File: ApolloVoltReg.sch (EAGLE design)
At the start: 24 parts, among them IC2 LM324D, J1 SSM-108-L-DV-BE-K-APOLLO, U1 TEXAS_INSTRUMENTS_PTH04070WAD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, U2 ACS712ELCTR-05B-T

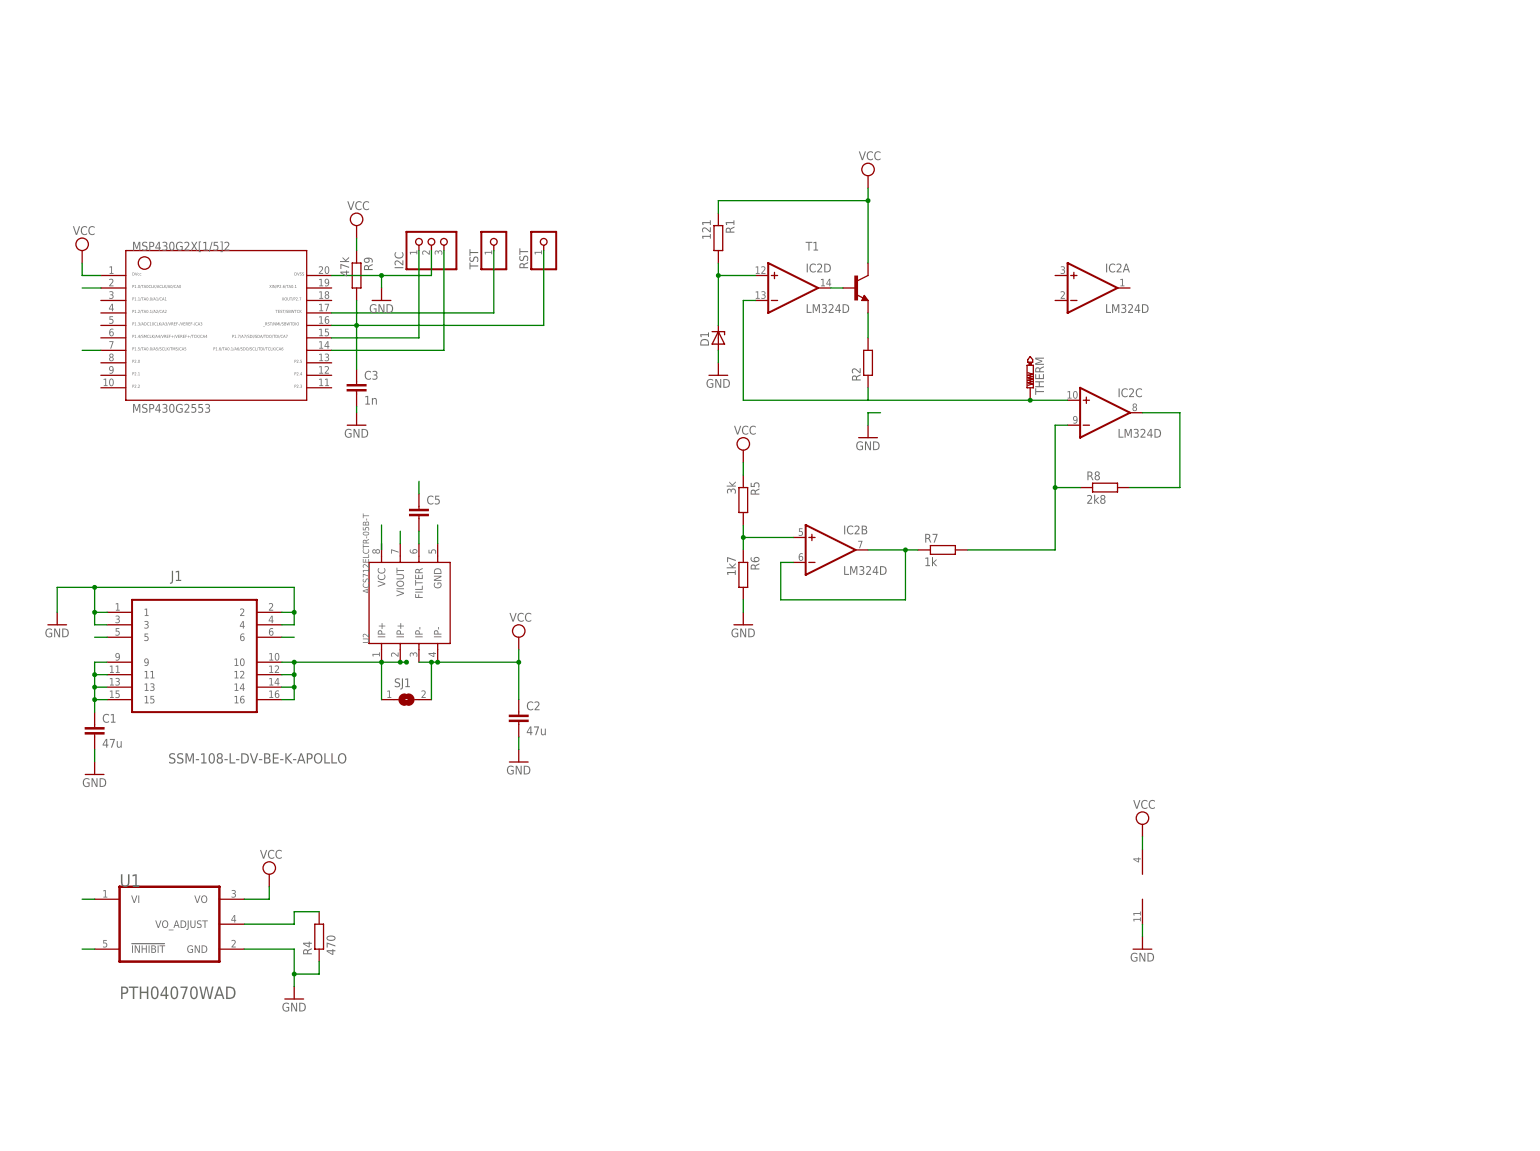
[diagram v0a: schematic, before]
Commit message: pcb cleanup overtemp-shutdown (optional) gerber files
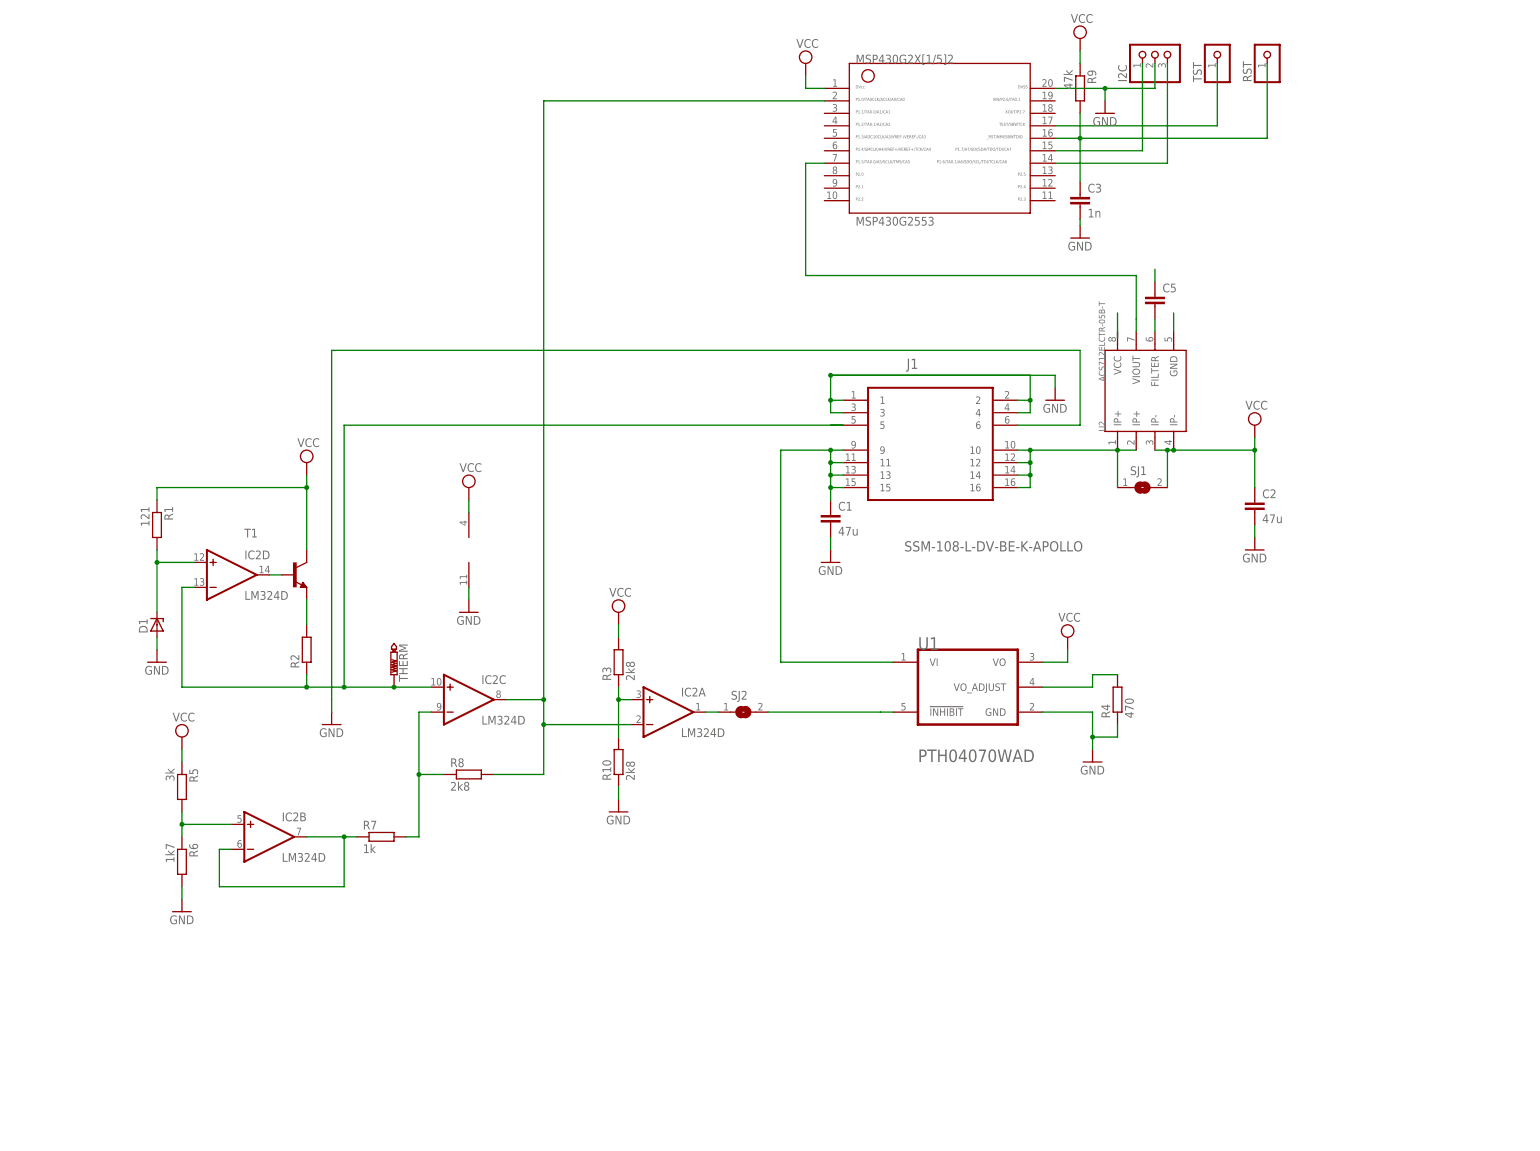
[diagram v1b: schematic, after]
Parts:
- added R10, R3: 2k8, resistor:R-EU_R0603
- added SJ2: (no value), jumper:SJ
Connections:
- removed net NC: U1.!INHIBIT!
- new net /INHIBIT: SJ2.2, U1.!INHIBIT!
- new net N$11: IC2A.+IN, R10.2, R3.1
- new net N$12: IC2A.OUT, SJ2.1
- new net THERM0: J1.6
- net GND: now also R10.1; no longer J1.6
- net TEMPSENS: now also IC2A.-IN
- net VCC: now also R3.2
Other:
- moved on the sheet: C1, C2, C3, C5, D1, I2C, IC2A, IC2B, IC2C, IC2D, J1, MSP430G2553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

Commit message: replace opamp with TL084D
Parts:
- IC2: value LM324D -> TL084D; device linear:LM324D -> linear:TL084D
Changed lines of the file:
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@@
 <part name="U1" library="Texas Instruments - PTH04070WAD" deviceset="TEXAS_INSTRUMENTS_PTH04070WAD" device="TEXAS_INSTRUMENTS_PTH04070WAD_0_0"/>
 <part name="R4" library="resistor" deviceset="R-EU_" device="R0603" value="470"/>
-<part name="IC2" library="linear" deviceset="LM324" device="D" value="LM324D"/>
+<part name="IC2" library="linear" deviceset="TL084" device="D" value="TL084D"/>
 <part name="D1" library="diode" deviceset="ZENER-DIODE" device="SOD80C"/>
 <part name="T1" library="transistor" deviceset="*-NPN-" device="SOT23-EBC"/>

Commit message: widen high current traces
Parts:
- C5: value (none) -> 100n
- R10: value 2k8 -> 20k
- R2: value (none) -> 840
- R3: value 2k8 -> 2k
- RST, TST: device adafruit:PINHD-1X1 -> adafruit:PINHD-1X1CB
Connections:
- removed net THERM0: J1.6
- net GND: now also J1.6
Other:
- moved on the sheet: C1, C2, C3, C5, D1, I2C, IC2A, IC2B, IC2C, IC2D, J1, MSP430G2553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

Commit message: gerber in archs
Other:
- moved on the sheet: C3, I2C, IC2B, MSP430G2553, R4, R5, R6, R8, R9, RST, TST

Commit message: adding pic
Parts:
- removed MSP430G2553: G2X[1/5]2---N20, TI_MSP430_v16:G2X[1/5]2---N20
- removed T1: (no value), transistor:-NPN-SOT23-EBC
- added D2: BAS40-06, diode:BAS40-06
- added FAN: (no value), pinhead:PINHD-1X2
- added IC1: MCP1703CB, linear:MCP1703CB
- added JLCJLCJLCJLC: G2X[1/5]2---N20, TI_MSP430_v16:G2X[1/5]2---N20
- added LED1: (no value), adafruit:LED3MM
- added Q1: (no value), semicon-smd-ipc:PNP-TRANSISTOR_SOT23
- added Q2: (no value), adafruit:MOSFET-NREFLOW
- added R11, R12, R13: 2k, resistor:R-EU_R0805
- added R14: 2k, resistor:R-EU_R0603
- added SJ3, SJ5: (no value), jumper:SJ2W
- C1, C2: device eagle-ltspice:CC1206 -> eagle-ltspice:CC1210
- D1: value (none) -> BAS40-04; device diode:ZENER-DIODESOD80C -> diode:BAS40-04
- I2C: device adafruit:PINHD-1X3 -> pinhead:PINHD-1X5
- R1: value 121 -> 1k; device resistor:R-EU_R0603 -> resistor:R-EU_R0805
- R10, R3, R4, R5, R6, R7, R8: device resistor:R-EU_R0603 -> resistor:R-EU_R0805
- R2: value 840 -> 1k3; device resistor:R-EU_R0603 -> resistor:R-EU_R0805
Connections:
- new net N$13: IC2D.-IN, R11.2, R14.2
- new net N$14: IC2D.OUT, R11.1, SJ3.1
- new net N$15: JLCJLCJLCJLC.7, SJ3.2
- new net N$16: IC1.VO, JLCJLCJLCJLC.1, R9.1, SJ5.2
- new net N$17: D2.K2, IC2A.OUT
- new net N$18: D2.AA, SJ2.1
- new net N$19: FAN.2, Q2.D
- new net N$21: I2C.3, SJ5.3
- new net RST: C3.1, JLCJLCJLCJLC.16, R9.2, RST.1
- net +5V: now also FAN.1, IC1.VI, IC2P.V+, LED1.A, R12.1, R2.2, R3.2, R5.1
- net ACS_OUT: now also R14.1, SJ3.3; no longer MSP430G2553.7
- net CPU: now also D1.C2
- net GND: now also D1.A1, I2C.1, I2C.5, IC1.GND, JLCJLCJLCJLC.20, Q2.S, R1.2, R13.2; no longer D1.A, I2C.2, MSP430G2553.20
- net N$10: now also JLCJLCJLCJLC.17; no longer MSP430G2553.17
- net N$12: now also D2.K1, JLCJLCJLCJLC.5; no longer IC2A.OUT, SJ2.1
- net N$2: now also LED1.C, Q1.B, R1.1; no longer D1.C, IC2D.+IN, R1.2
- net N$3: now also Q1.E, R2.1; no longer IC2D.OUT, T1.B
- net N$4: now also IC2D.+IN, R12.2, R13.1; no longer R2.2, T1.E
- net N$9: now also JLCJLCJLCJLC.19, Q2.G; no longer C3.1, MSP430G2553.16, R9.2, RST.1
- net SCL: now also I2C.4, JLCJLCJLCJLC.14; no longer I2C.3, MSP430G2553.14
- net SDA: now also I2C.2, JLCJLCJLCJLC.15; no longer I2C.1, MSP430G2553.15
- net TEMPSENS: now also JLCJLCJLCJLC.2; no longer MSP430G2553.2
- net THERM1: now also D1.C1A2, Q1.C; no longer IC2D.-IN, R2.1
- net VCC: now also SJ5.1; no longer IC2P.V+, MSP430G2553.1, R1.1, R3.2, R5.1, R9.1, T1.C
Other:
- moved on the sheet: C1, C2, C3, C5, IC2A, IC2B, IC2C, IC2D, J1, R1, R10, R2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
